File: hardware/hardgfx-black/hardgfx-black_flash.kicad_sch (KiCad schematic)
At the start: 13 parts, among them U5 MT25QL512ABB8ESF-0AAT, U6 MT25QL512ABB8ESF-0AAT

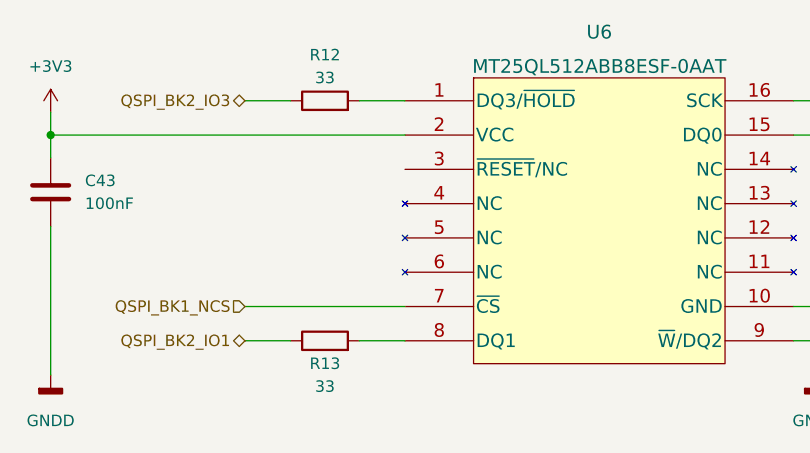
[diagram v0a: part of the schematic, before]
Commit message: Finish first schematic version.
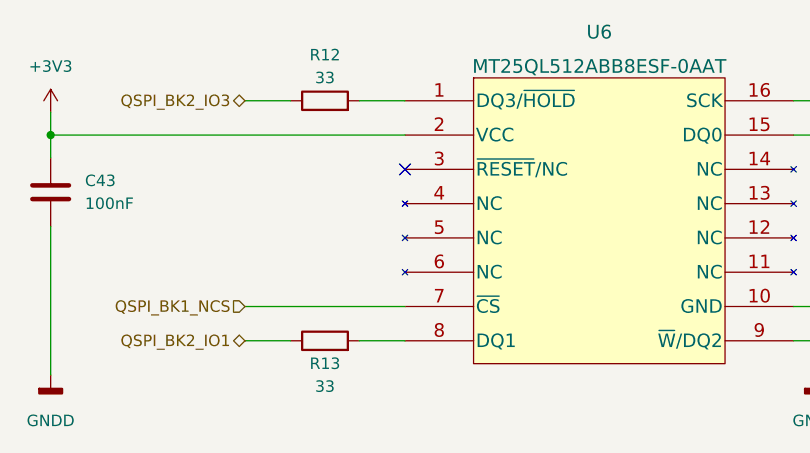
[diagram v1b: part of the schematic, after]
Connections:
- no-connect marks 1 -> 2
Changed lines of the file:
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@@
   (junction (at 35.56 64.77) (diameter 0) (color 0 0 0 0)
   )
+  (no_connect (at 204.47 68.58))
   (no_connect (at 74.93 68.58))
   (wire (pts (xy 67.31 64.77) (xy 67.31 72.39))

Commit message: J12 connector symbol and footprint modified. Previous J12 connector had incorrect connections.
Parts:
- U5, U6: footprint MT25QL512ABB8ESF-0AAT:MT25QL512ABB8ESF-0AAT -> Package_SO:SOIC-16W_7.5x10.3mm_P1.27mm
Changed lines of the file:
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@@
       (effects (font (size 1.524 1.524)))
     )
-    (property "Footprint" "MT25QL512ABB8ESF-0AAT:MT25QL512ABB8ESF-0AAT" (id 2) (at 226.06 54.864 0)
+    (property "Footprint" "Package_SO:SOIC-16W_7.5x10.3mm_P1.27mm" (id 2) (at 226.06 54.864 0)
       (effects (font (size 1.524 1.524)) hide)
     )
@@
       (effects (font (size 1.524 1.524)))
     )
-    (property "Footprint" "MT25QL512ABB8ESF-0AAT:MT25QL512ABB8ESF-0AAT" (id 2) (at 96.52 54.864 0)
+    (property "Footprint" "Package_SO:SOIC-16W_7.5x10.3mm_P1.27mm" (id 2) (at 96.52 54.864 0)
       (effects (font (size 1.524 1.524)) hide)
     )

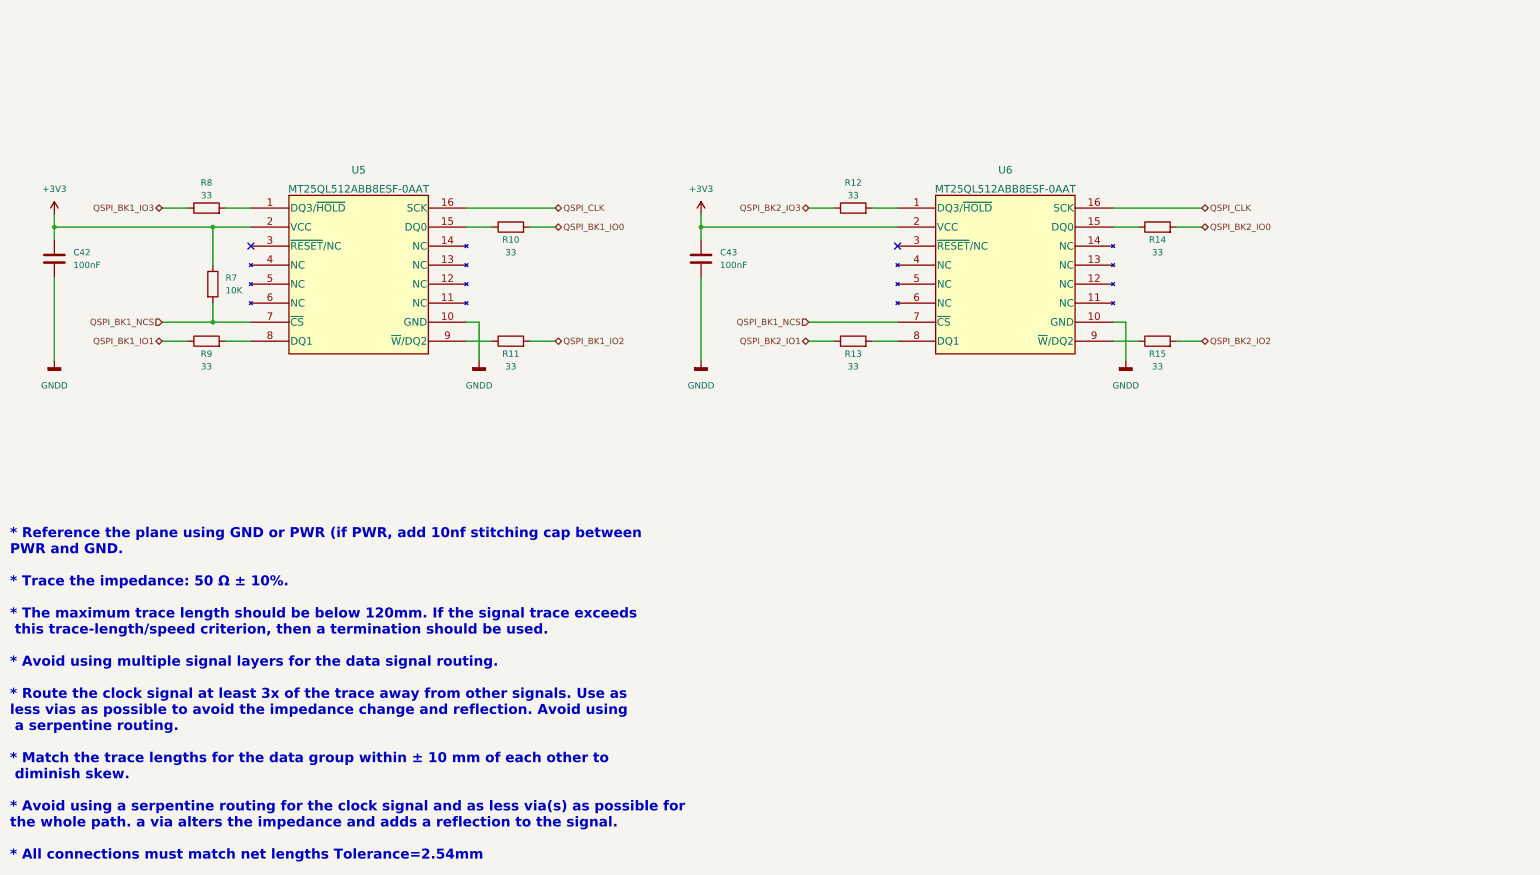
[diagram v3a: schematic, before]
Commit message: Added generic SDRAM configuration using macros.
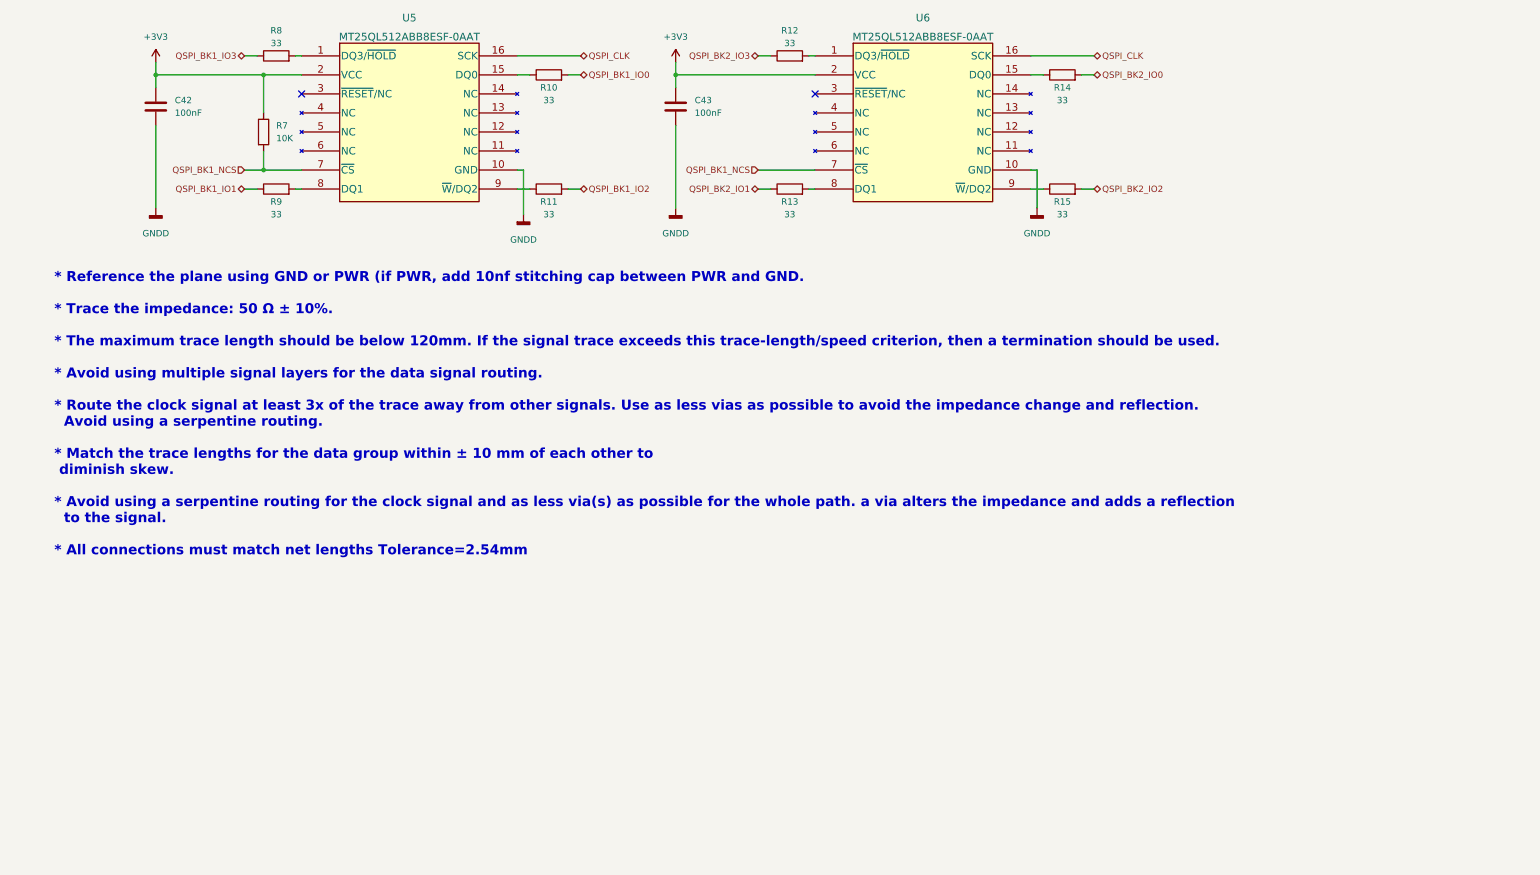
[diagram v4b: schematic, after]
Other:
- moved on the sheet: C42, C43, R10, R11, R12, R13, R14, R15, R7, R8, R9, U5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
